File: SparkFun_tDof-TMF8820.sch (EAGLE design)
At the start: 28 parts, among them J4 QWIIC_RIGHT_ANGLE, J5 QWIIC_RIGHT_ANGLE

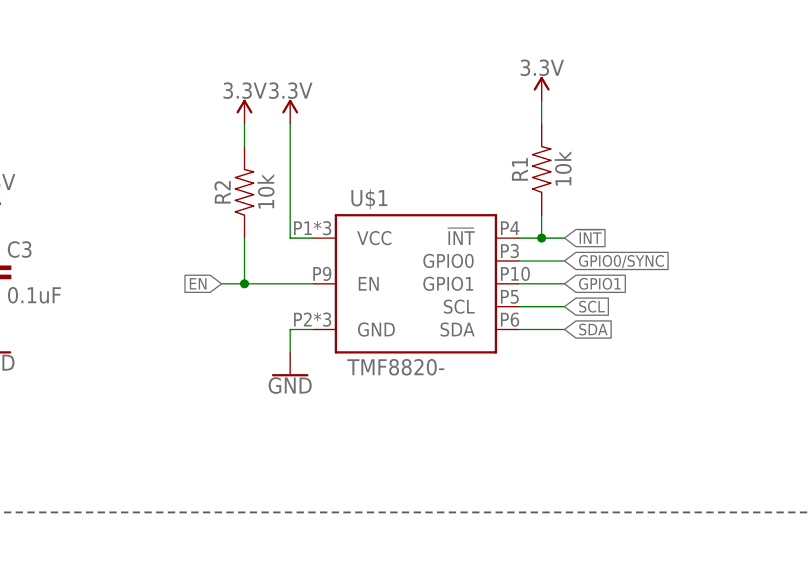
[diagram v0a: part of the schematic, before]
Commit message: Adds silk to TMF8820, updates footprint with pin 1 indicator
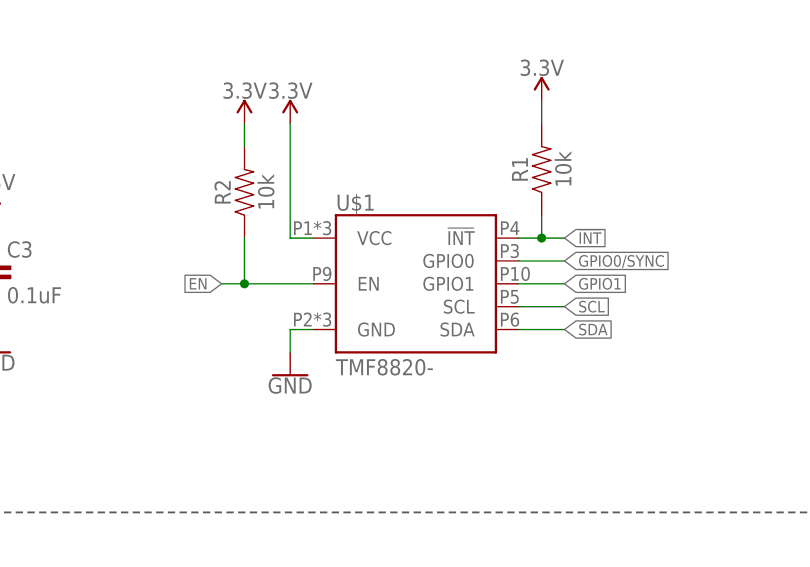
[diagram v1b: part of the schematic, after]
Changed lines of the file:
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@@
 </instance>
 <instance part="U$1" gate="G$1" x="99.06" y="129.54" smashed="yes">
-<attribute name="NAME" x="90.424" y="138.176" size="1.778" layer="95" font="vector"/>
-<attribute name="VALUE" x="90.17" y="119.38" size="1.778" layer="96" font="vector"/>
+<attribute name="NAME" x="88.9" y="137.668" size="1.778" layer="95" font="vector"/>
+<attribute name="VALUE" x="88.9" y="119.38" size="1.778" layer="96" font="vector"/>
 </instance>
 <instance part="C1" gate="G$1" x="25.4" y="129.54" smashed="yes">
